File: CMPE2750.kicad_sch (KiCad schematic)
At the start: 50 parts, among them J1 Conn_02x07_Odd_Even, J2 SPI3, J3 Conn_02x16_Top_Bottom, J4 Conn_01x16, J5 Conn_01x04, SW1 D6R90F1LFS, U1 STM32L476RGTx, X1 ABS25-32.768KHZ-6-T

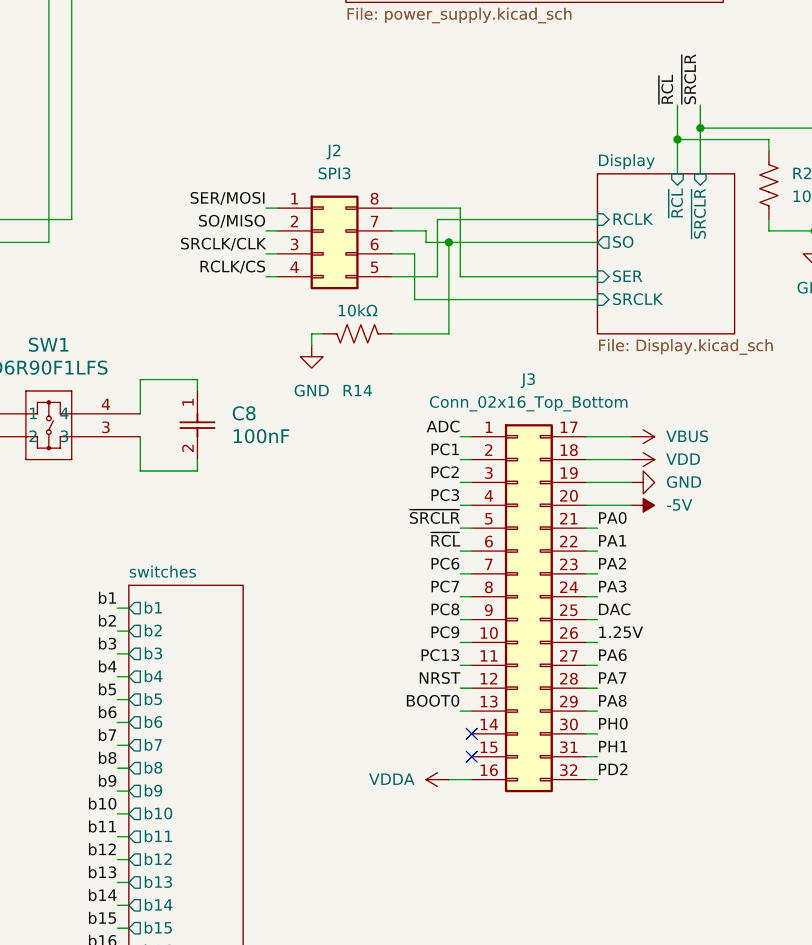
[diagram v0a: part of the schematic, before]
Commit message: Component placing partly done. Saving before overwriting the pcb with the templating script output
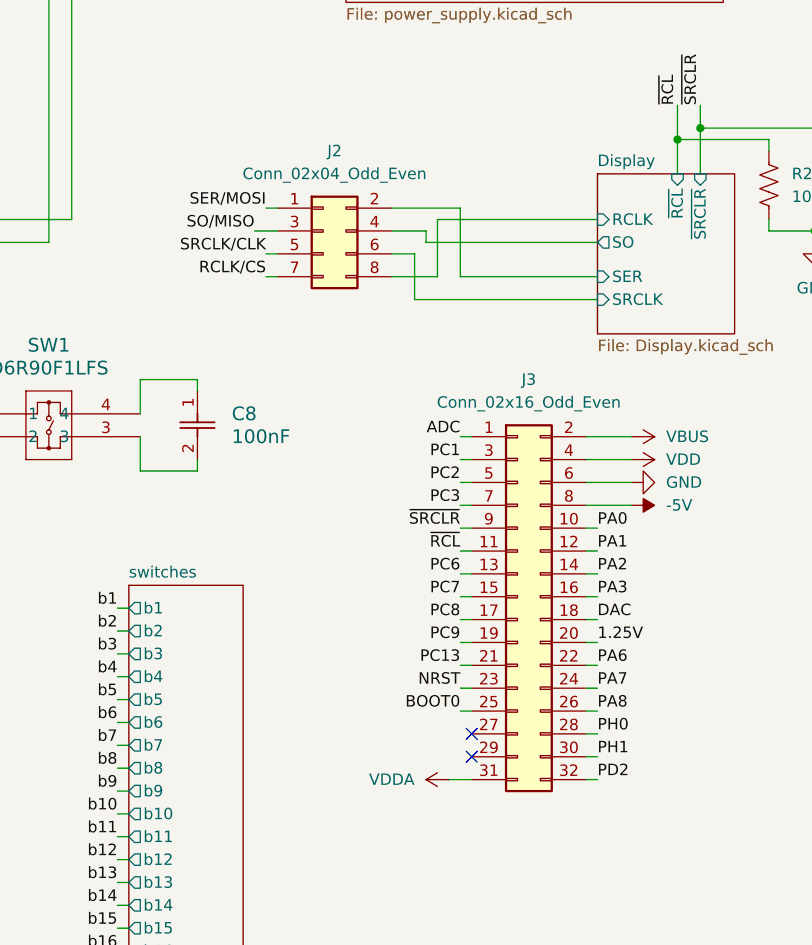
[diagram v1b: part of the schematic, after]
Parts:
- removed R14: 10kΩ, Resistor_SMD:R_0402_1005Metric, symbol CMPE2750:0402WGJ0103TCE
- J2: value SPI3 -> Conn_02x04_Odd_Even; symbol Connector_Generic:Conn_02x04_Counter_Clockwise -> Connector_Generic:Conn_02x04_Odd_Even
- J3: value Conn_02x16_Top_Bottom -> Conn_02x16_Odd_Even; footprint Connector_PinHeader_2.54mm:PinHeader_2x06_P2.54mm_Vertical -> Connector_PinHeader_2.54mm:PinHeader_2x16_P2.54mm_Vertical; symbol Connector_Generic:Conn_02x16_Top_Bottom -> Connector_Generic:Conn_02x16_Odd_Even
- J4: footprint Connector_PinHeader_2.54mm:PinHeader_1x06_P2.54mm_Vertical -> Connector_PinHeader_2.54mm:PinHeader_1x16_P2.54mm_Vertical
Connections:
- net -5V: now also J3.8 (Pin_8); no longer J3.20 (Pin_20)
- net 1.25V: now also J3.20 (Pin_20); no longer J3.26 (Pin_26)
- net BOOT0: now also J3.25 (Pin_25); no longer J3.13 (Pin_13)
- net DAC: now also J3.18 (Pin_18); no longer J3.25 (Pin_25)
- net Display/RCLK: now also J2.8 (Pin_8); no longer J2.5 (Pin_5)
- net Display/SER: now also J2.2 (Pin_2); no longer J2.8 (Pin_8)
- net Display/SO: now also J2.4 (Pin_4); no longer J2.7 (Pin_7)
- net GND: now also J3.6 (Pin_6); no longer J3.19 (Pin_19)
- net NRST: now also J3.23 (Pin_23); no longer J3.12 (Pin_12)
- net PA0: now also J3.10 (Pin_10); no longer J3.21 (Pin_21)
- net PA1: now also J3.12 (Pin_12); no longer J3.22 (Pin_22)
- net PA2: now also J3.14 (Pin_14); no longer J3.23 (Pin_23)
- net PA3: now also J3.16 (Pin_16); no longer J3.24 (Pin_24)
- net PA6: now also J3.22 (Pin_22); no longer J3.27 (Pin_27)
- net PA7: now also J3.24 (Pin_24); no longer J3.28 (Pin_28)
- net PA8: now also J3.26 (Pin_26); no longer J3.29 (Pin_29)
- net PC1: now also J3.3 (Pin_3); no longer J3.2 (Pin_2)
- net PC13: now also J3.21 (Pin_21); no longer J3.11 (Pin_11)
- net PC2: now also J3.5 (Pin_5); no longer J3.3 (Pin_3)
- net PC3: now also J3.7 (Pin_7); no longer J3.4 (Pin_4)
- net PC6: now also J3.13 (Pin_13); no longer J3.7 (Pin_7)
- net PC7: now also J3.15 (Pin_15); no longer J3.8 (Pin_8)
- net PC8: now also J3.17 (Pin_17); no longer J3.9 (Pin_9)
- net PC9: now also J3.19 (Pin_19); no longer J3.10 (Pin_10)
- net PH0: now also J3.28 (Pin_28); no longer J3.30 (Pin_30)
- net PH1: now also J3.30 (Pin_30); no longer J3.31 (Pin_31)
- net RCLK/CS: now also J2.7 (Pin_7); no longer J2.4 (Pin_4)
- net SO/MISO: now also J2.3 (Pin_3); no longer J2.2 (Pin_2)
- net SRCLK/CLK: now also J2.5 (Pin_5); no longer J2.3 (Pin_3)
- net VBUS: now also J3.2 (Pin_2); no longer J3.17 (Pin_17)
- net VDD: now also J3.4 (Pin_4); no longer J3.18 (Pin_18)
- net VDDA: now also J3.31 (Pin_31); no longer J3.16 (Pin_16)
- net ~{RCL}: now also J3.11 (Pin_11); no longer J3.6 (Pin_6)
- net ~{SRCLR}: now also J3.9 (Pin_9); no longer J3.5 (Pin_5)
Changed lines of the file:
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@@
 	)
 	(junction
-		(at 186.69 96.52)
-		(diameter 0)
-		(color 0 0 0 0)
-	)
-	(junction
 		(at 45.72 36.83)
 		(diameter 0)
@@
 	(wire
 		(pts
-			(xy 171.45 106.68) (xy 171.45 107.95)
-		)
-		(stroke
-			(width 0)
-			(type default)
-		)
-	)
-	(wire
-		(pts
 			(xy 184.15 96.52) (xy 184.15 95.25)
 		)
@@
 	(wire
 		(pts
+			(xy 187.96 100.33) (xy 203.2 100.33)
+		)
+		(stroke
+			(width 0)
+			(type default)
+		)
+	)
+	(wire
+		(pts
 			(xy 115.57 172.72) (xy 116.84 172.72)
 		)
@@
 	(wire
 		(pts
-			(xy 203.2 96.52) (xy 186.69 96.52)
+			(xy 184.15 96.52) (xy 203.2 96.52)
 		)
 		(stroke
@@
 	(wire
 		(pts
-			(xy 203.2 102.87) (xy 182.88 102.87)
-		)
-		(stroke
-			(width 0)
-			(type default)
-		)
-	)
-	(wire
-		(pts
 			(xy 248.92 86.36) (xy 248.92 80.01)
 		)
@@
 	(wire
 		(pts
-			(xy 186.69 106.68) (xy 186.69 96.52)
+			(xy 83.82 55.88) (xy 83.82 31.75)
 		)
 		(stroke
@@
 	(wire
 		(pts
-			(xy 83.82 55.88) (xy 83.82 31.75)
+			(xy 95.25 137.16) (xy 93.98 137.16)
 		)
 		(stroke
@@
 	(wire
 		(pts
-			(xy 95.25 137.16) (xy 93.98 137.16)
+			(xy 57.15 99.06) (xy 58.42 99.06)
 		)
 		(stroke
@@
 	(wire
 		(pts
-			(xy 57.15 99.06) (xy 58.42 99.06)
+			(xy 185.42 93.98) (xy 203.2 93.98)
 		)
 		(stroke
@@
 	(wire
 		(pts
-			(xy 203.2 93.98) (xy 185.42 93.98)
+			(xy 57.15 73.66) (xy 58.42 73.66)
 		)
 		(stroke
@@
 	(wire
 		(pts
-			(xy 57.15 73.66) (xy 58.42 73.66)
+			(xy 165.1 95.25) (xy 167.64 95.25)
 		)
 		(stroke
@@
 	(wire
 		(pts
-			(xy 166.37 95.25) (xy 167.64 95.25)
+			(xy 187.96 143.51) (xy 189.23 143.51)
 		)
 		(stroke
@@
 	(wire
 		(pts
-			(xy 187.96 143.51) (xy 189.23 143.51)
+			(xy 182.88 102.87) (xy 203.2 102.87)
 		)
 		(stroke
@@
 	(wire
 		(pts
-			(xy 186.69 96.52) (xy 184.15 96.52)
-		)
-		(stroke
-			(width 0)
-			(type default)
-		)
-	)
-	(wire
-		(pts
 			(xy 69.85 31.75) (xy 83.82 31.75)
 		)
@@
 	(wire
 		(pts
-			(xy 172.72 106.68) (xy 171.45 106.68)
-		)
-		(stroke
-			(width 0)
-			(type default)
-		)
-	)
-	(wire
-		(pts
 			(xy 95.25 124.46) (xy 93.98 124.46)
 		)
@@
 	(wire
 		(pts
-			(xy 180.34 106.68) (xy 186.69 106.68)
-		)
-		(stroke
-			(width 0)
-			(type default)
-		)
-	)
-	(wire
-		(pts
 			(xy 172.72 59.69) (xy 175.26 59.69)
 		)
@@
 	(wire
 		(pts
-			(xy 203.2 100.33) (xy 187.96 100.33)
-		)
-		(stroke
-			(width 0)
-			(type default)
-		)
-	)
-	(wire
-		(pts
 			(xy 95.25 134.62) (xy 93.98 134.62)
 		)
@@
 	)
 	(label "SO/MISO"
-		(at 166.37 95.25 180)
+		(at 165.1 95.25 180)
 		(fields_autoplaced yes)
 		(effects
@@
 	)
 	(symbol
-		(lib_id "Connector_Generic:Conn_02x16_Top_Bottom")
+		(lib_id "Connector_Generic:Conn_02x16_Odd_Even")
 		(at 194.31 135.89 0)
 		(unit 1)
@@
 			)
 		)
-		(property "Value" "Conn_02x16_Top_Bottom"
+		(property "Value" "Conn_02x16_Odd_Even"
 			(at 195.58 114.3 0)
 			(effects
@@
 			)
 		)
-		(property "Footprint" "Connector_PinHeader_2.54mm:PinHeader_2x06_P2.54mm_Vertical"
+		(property "Footprint" "Connector_PinHeader_2.54mm:PinHeader_2x16_P2.54mm_Vertical"
 			(at 194.31 135.89 0)
 			(effects
@@
 			)
 		)
-		(property "Description" "Generic connector, double row, 02x16, top/bottom pin numbering scheme (row 1: 1...pins_per_row, row2: pins_per_row+1 ... num_pins), script generated (kicad-library-utils/schlib/autogen/connector/)"
+		(property "Description" "Generic connector, double row, 02x16, odd/even pin numbering scheme (row 1 odd numbers, row 2 even numbers), script generated (kicad-library-utils/schlib/autogen/connector/)"
 			(at 194.31 135.89 0)
 			(effects
@@
 	)
 	(symbol
-		(lib_id "CMPE2750:0402WGJ0103TCE")
-		(at 176.53 106.68 90)
-		(mirror x)
-		(unit 1)
-		(exclude_from_sim no)
-		(in_bom yes)
-		(on_board yes)
-		(dnp no)
-		(property "Reference" "R14"
-			(at 176.53 113.03 90)
-			(effects
-				(font
-					(size 1.27 1.27)
-				)
-			)
-		)
-		(property "Value" "10kΩ"
-			(at 176.53 104.14 90)
-			(effects
-				(font
-					(size 1.27 1.27)
-				)
-			)
-		)
-		(property "Footprint" "Resistor_SMD:R_0402_1005Metric"
-			(at 176.784 107.696 90)
-			(effects
-				(font
-					(size 1.27 1.27)
-				)
-				(hide yes)
-			)
-		)
-		(property "Datasheet" "0402WGJ0103TCE"
-			(at 176.53 106.68 0)
-			(effects
-				(font
-					(size 1.27 1.27)
-				)
-				(hide yes)
-			)
-		)
-		(property "Description" "Resistor, US symbol"
-			(at 176.53 106.68 0)
-			(effects
-				(font
-					(size 1.27 1.27)
-				)
-				(hide yes)
-			)
-		)
-		(pin "1"
-		)
-		(pin "2"
-		)
-		(instances
-			(project "CMPE2750"
-				(path "/a86318a1-888d-4137-89a5-221e5a1bc171"
-					(reference "R14")
-					(unit 1)
-				)
-			)
-		)
-	)
-	(symbol
 		(lib_id "power:GND")
 		(at 269.24 99.06 0)
@@
 	)
 	(symbol
-		(lib_id "Connector_Generic:Conn_02x04_Counter_Clockwise")
+		(lib_id "Connector_Generic:Conn_02x04_Odd_Even")
 		(at 172.72 95.25 0)
 		(unit 1)
@@
 			)
 		)
-		(property "Value" "SPI3"
+		(property "Value" "Conn_02x04_Odd_Even"
 			(at 173.99 88.9 0)
 			(effects
@@
 			)
 		)
-		(property "Description" "Generic connector, double row, 02x04, counter clockwise pin numbering scheme (similar to DIP package numbering), script generated (kicad-library-utils/schlib/autogen/connector/)"
+		(property "Description" "Generic connector, double row, 02x04, odd/even pin numbering scheme (row 1 odd numbers, row 2 even numbers), script generated (kicad-library-utils/schlib/autogen/connector/)"
 			(at 172.72 95.25 0)
 			(effects
@@
 			)
 		)
-		(property "Footprint" "Connector_PinHeader_2.54mm:PinHeader_1x06_P2.54mm_Vertical"
+		(property "Footprint" "Connector_PinHeader_2.54mm:PinHeader_1x16_P2.54mm_Vertical"
 			(at 121.92 162.56 0)
 			(effects
@@
 					(unit 1)
 				)
-			)
-		)
-	)
-	(symbol
-		(lib_id "power:GND")
-		(at 171.45 107.95 0)
-		(unit 1)
-		(exclude_from_sim no)
-		(in_bom yes)
-		(on_board yes)
-		(dnp no)
-		(fields_autoplaced yes)
-		(property "Reference" "#PWR020"
-			(at 171.45 114.3 0)
-			(effects
-				(font
-					(size 1.27 1.27)
-				)
-				(hide yes)
-			)
-		)
-		(property "Value" "GND"
-			(at 171.45 113.03 0)
-			(effects
-				(font
-					(size 1.27 1.27)
-				)
-			)
-		)
-		(property "Footprint" ""
-			(at 171.45 107.95 0)
-			(effects
-				(font
-					(size 1.27 1.27)
-				)
-				(hide yes)
-			)
-		)
-		(property "Datasheet" ""
-			(at 171.45 107.95 0)
-			(effects
-				(font
-					(size 1.27 1.27)
-				)
-				(hide yes)
-			)
-		)
-		(property "Description" "Power symbol creates a global label with name \"GND\" , ground"
-			(at 171.45 107.95 0)
-			(effects
-				(font
-					(size 1.27 1.27)
-				)
-				(hide yes)
-			)
-		)
-		(pin "1"
-		)
-		(instances
-			(project "CMPE2750"
-				(path "/a86318a1-888d-4137-89a5-221e5a1bc171"
-					(reference "#PWR020")
-					(unit 1)
-				)

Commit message: pcb almost done, just need to do the final copper fill
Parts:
- added C32, C33: 1.6nF, Capacitor_SMD:C_0805_2012Metric, symbol Device:C
- C6, C7: value 3.8 pF -> 5pF
- J1: footprint Connector_PinHeader_1.27mm:PinHeader_2x07_P1.27mm_Vertical -> CMPE2750:CONN_FTSH-107-01-F-DV-K-P-TR_SAI
- J5: footprint Connector_PinHeader_2.54mm:PinHeader_1x04_P2.54mm_Vertical -> Connector_PinHeader_2.54mm:PinHeader_1x06_P2.54mm_Vertical; symbol Connector_Generic:Conn_01x04 -> Connector_Generic:Conn_01x06
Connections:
- net MAIN_INPUT+: now also C32.1
- net MAIN_INPUT-: now also C33.1
- new net: C32.2, J5.5 (Pin_5)
- new net: C33.2, J5.6 (Pin_6)

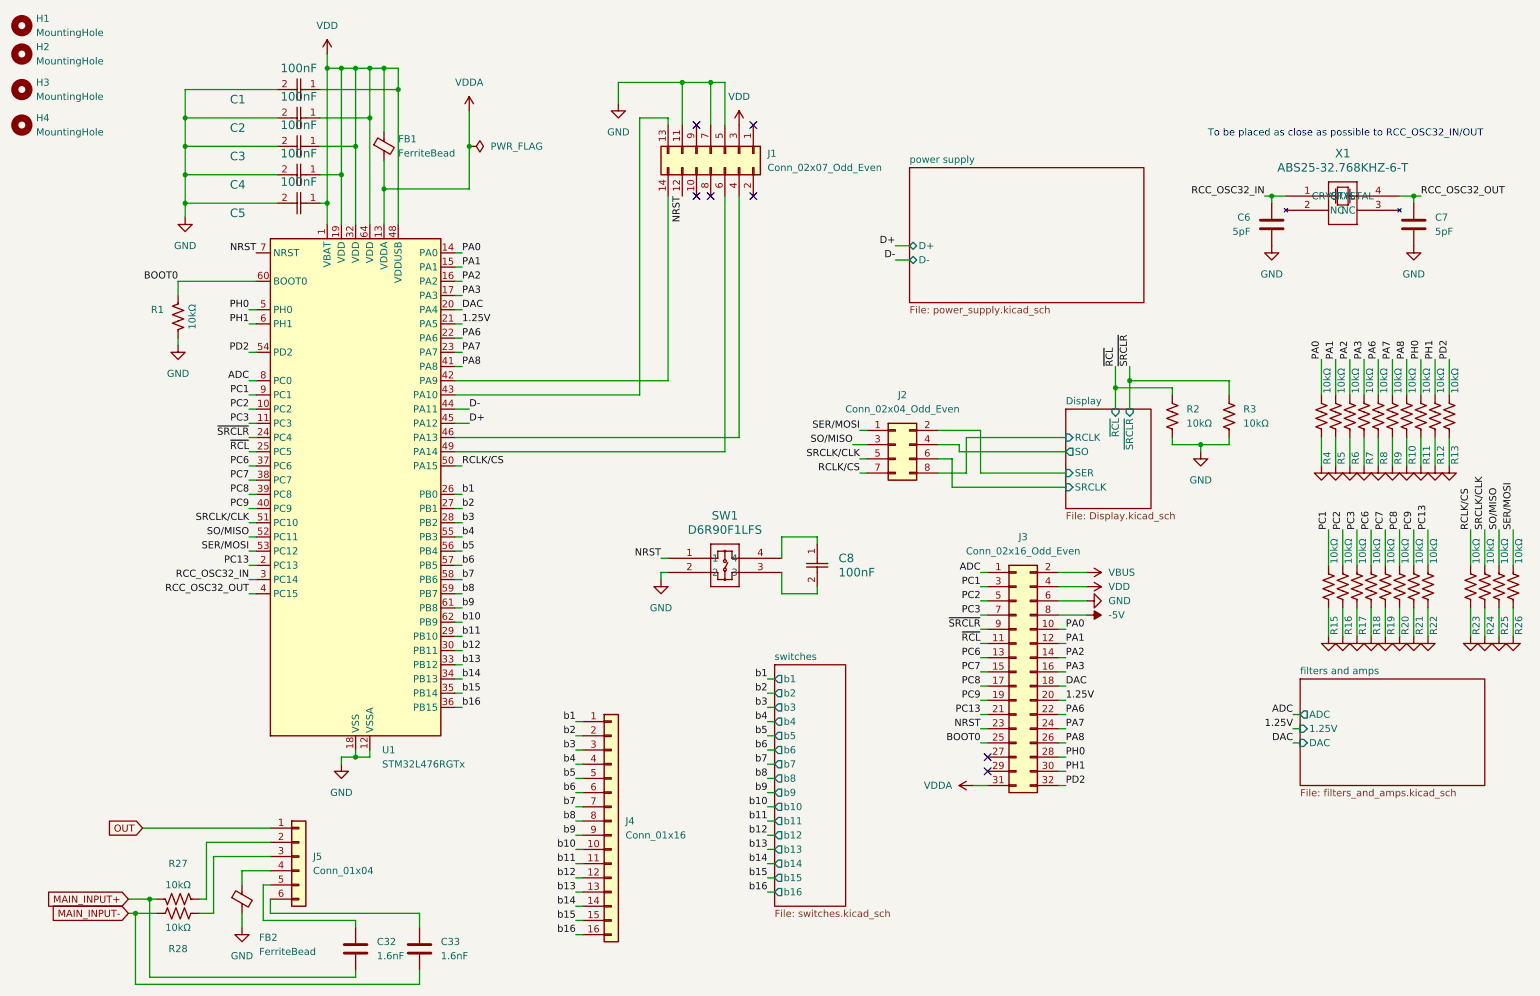
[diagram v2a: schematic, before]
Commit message: Made the final fills and the drill files
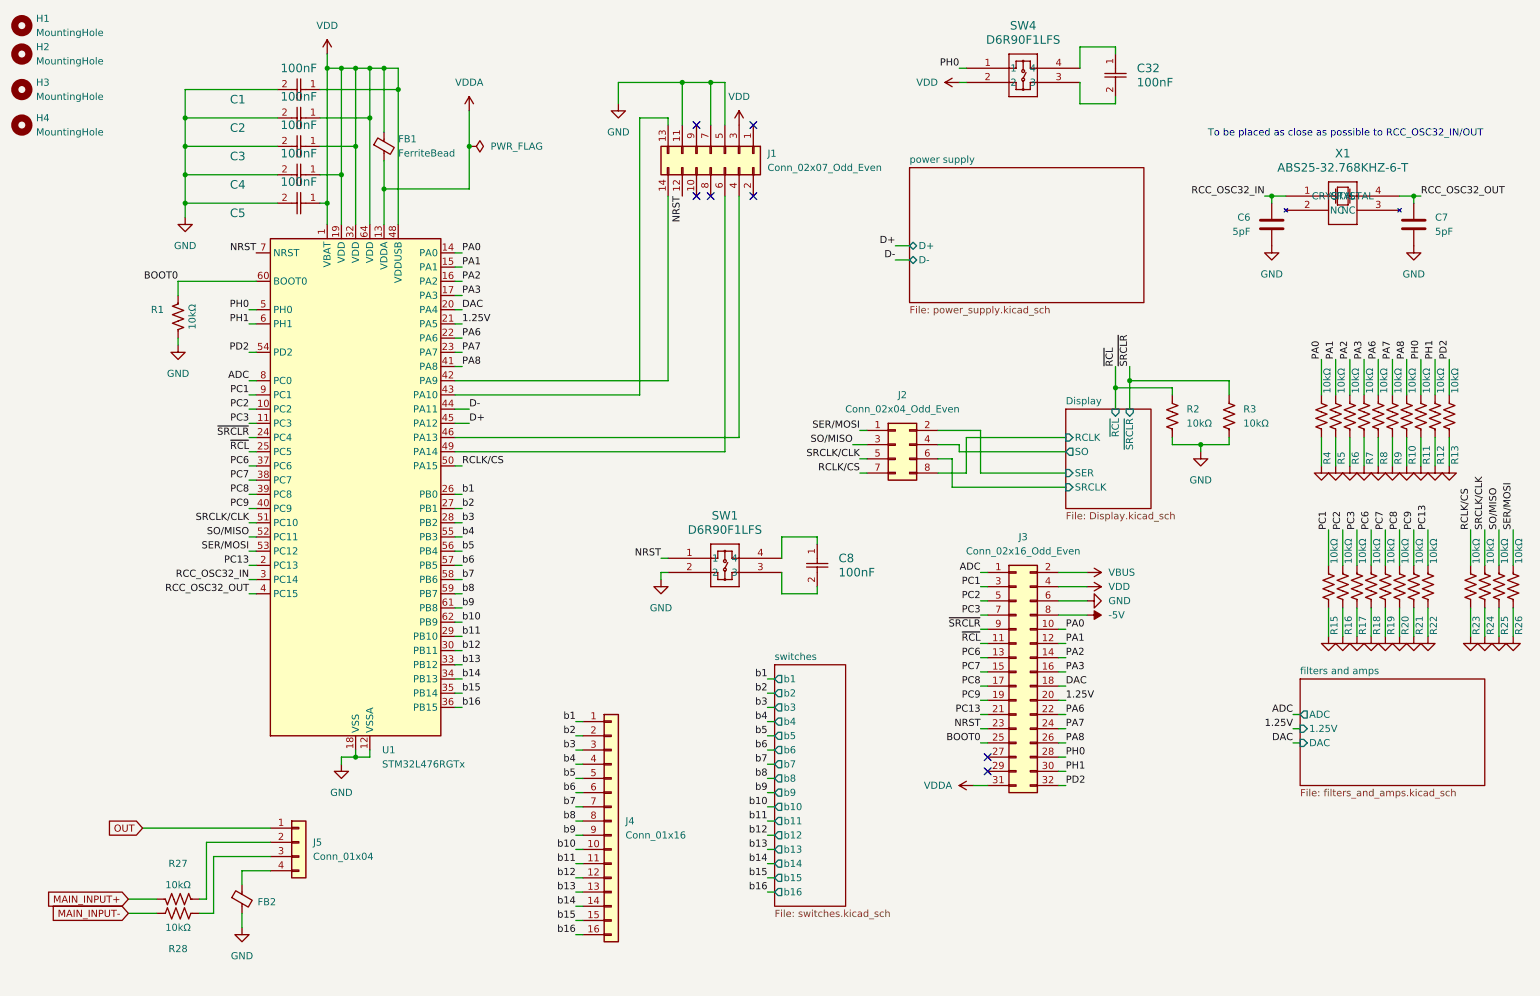
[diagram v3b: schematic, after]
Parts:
- removed C32, C33: 1.6nF, Capacitor_SMD:C_0805_2012Metric, symbol Device:C
- added C32: 100nF, Capacitor_SMD:C_0402_1005Metric, symbol CMPE2750:CL05B104KP5NNNC
- added SW4: D6R90F1LFS, CMPE2750:D6R_CNK, symbol CMPE2750:D6R90F1LFS
- J5: footprint Connector_PinHeader_2.54mm:PinHeader_1x06_P2.54mm_Vertical -> Connector_PinHeader_2.54mm:PinHeader_1x04_P2.54mm_Vertical; symbol Connector_Generic:Conn_01x06 -> Connector_Generic:Conn_01x04
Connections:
- net PH0: now also SW4.1
- net VDD: now also SW4.2
- new net: C32.1, SW4.4
- new net: C32.2, SW4.3

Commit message: finished
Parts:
- added D19: CUS520,H3F, Diode_SMD:D_SOD-323, symbol Device:D_Schottky
- added R39: 10kΩ, Resistor_SMD:R_0402_1005Metric, symbol CMPE2750:0402WGJ0103TCE
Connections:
- net ADC: now also R39.1; no longer U1.8 (PC0)
- net GND: now also D19.2 (A)
- new net: D19.1 (K), R39.2, U1.8 (PC0)
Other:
- sheet filters and amps ports: added CLK_{filt}; removed none
